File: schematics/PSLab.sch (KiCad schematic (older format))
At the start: 76 parts, among them J1 Programmer, J10 GND, J11 Vbus, J13 D+, J14 D-, J15 External Power, J16 I2C-2, J2 DoublePins, J5 Bluetooth, J6 I2C-1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

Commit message: fix: fiducials for production
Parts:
- TP5, TP6, TP7: footprint Fiducial:Fiducial_0.5mm_Mask1mm -> Fiducial:Fiducial_1mm_Mask2mm
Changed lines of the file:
@@
 F 0 "TP5" V 9731 6083 47  0000 L CNN
 F 1 "Fiducial" V 9818 6083 47  0000 L CNN
-F 2 "Fiducial:Fiducial_0.5mm_Mask1mm" H 9775 6005 60  0001 C CNN
+F 2 "Fiducial:Fiducial_1mm_Mask2mm" H 9775 6005 60  0001 C CNN
 F 3 "" H 9775 6005 60  0001 C CNN
 	1    9775 6005
@@
 F 0 "TP6" V 10176 6083 47  0000 L CNN
 F 1 "Fiducial" V 10263 6083 47  0000 L CNN
-F 2 "Fiducial:Fiducial_0.5mm_Mask1mm" H 10220 6005 60  0001 C CNN
+F 2 "Fiducial:Fiducial_1mm_Mask2mm" H 10220 6005 60  0001 C CNN
 F 3 "" H 10220 6005 60  0001 C CNN
 	1    10220 6005
@@
 F 0 "TP7" V 10626 6083 47  0000 L CNN
 F 1 "Fiducial" V 10713 6083 47  0000 L CNN
-F 2 "Fiducial:Fiducial_0.5mm_Mask1mm" H 10670 6005 60  0001 C CNN
+F 2 "Fiducial:Fiducial_1mm_Mask2mm" H 10670 6005 60  0001 C CNN
 F 3 "" H 10670 6005 60  0001 C CNN
 	1    10670 6005

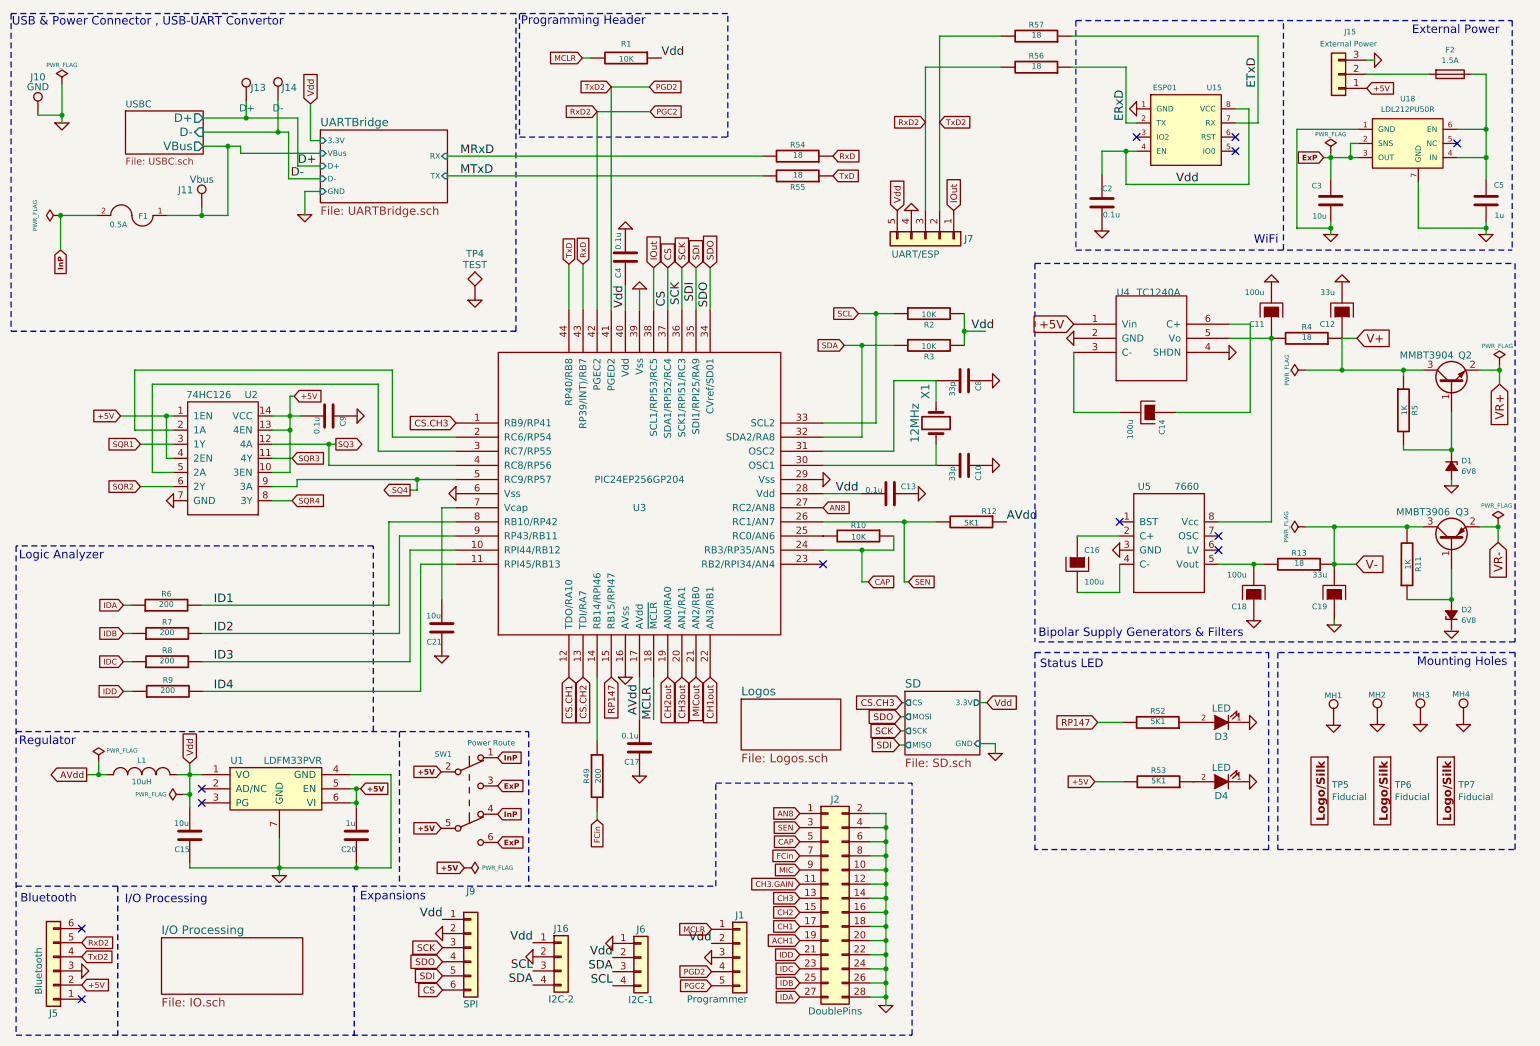
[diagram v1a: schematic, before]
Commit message: fix: line issues in uart ic for external power
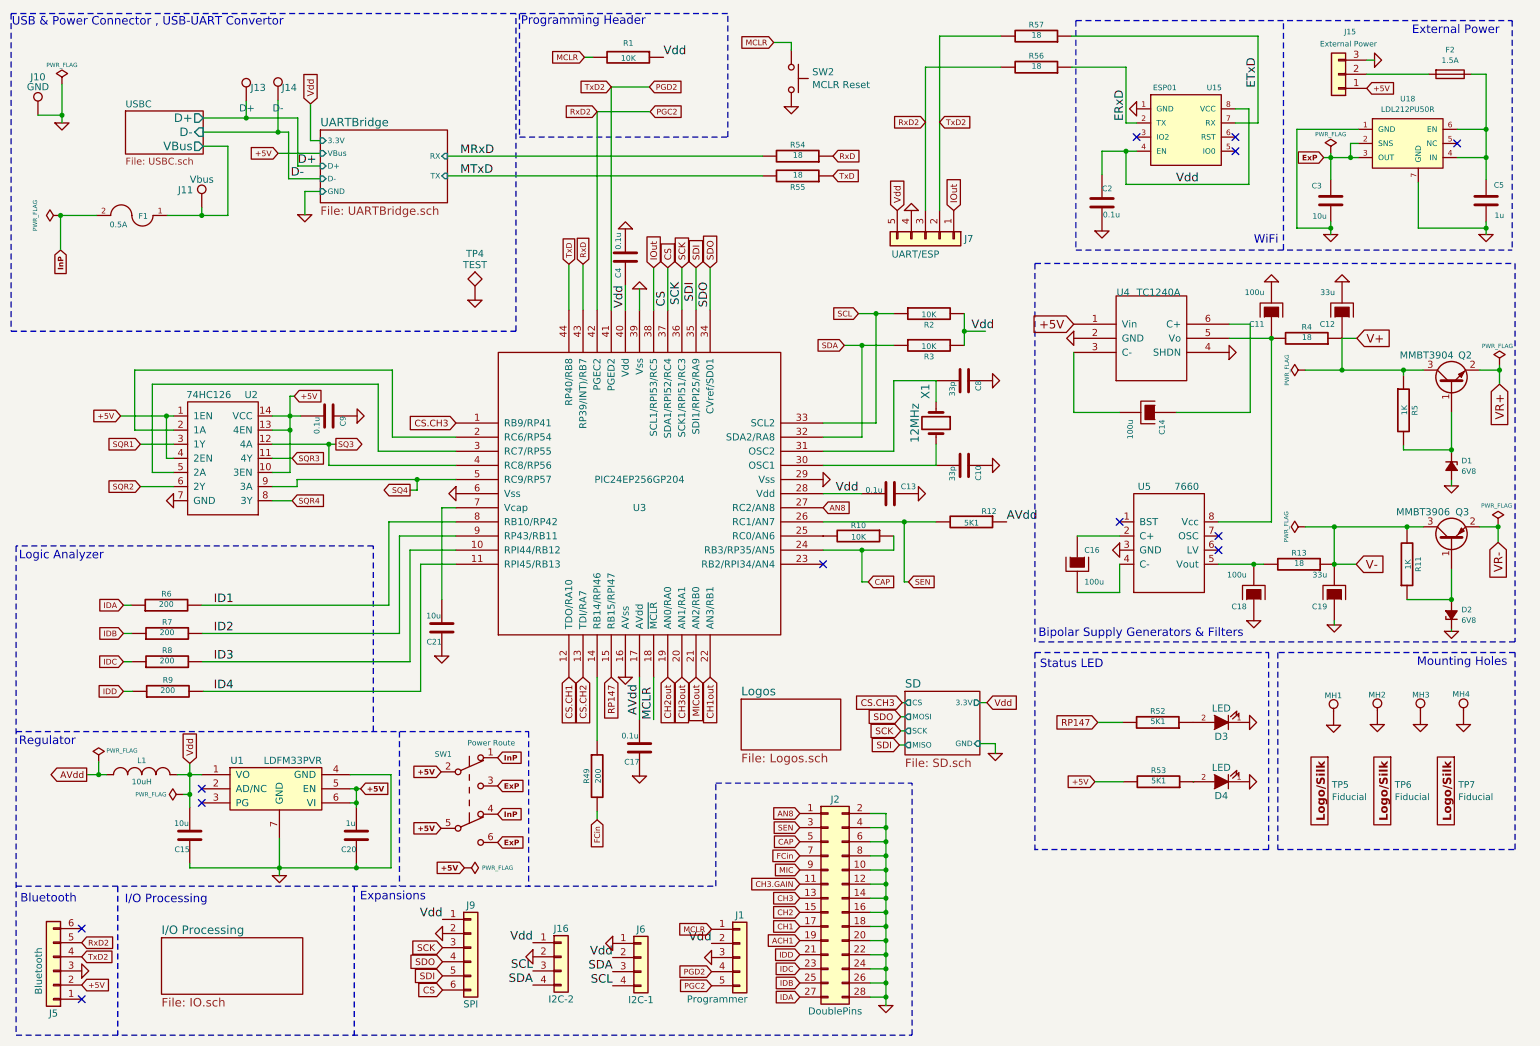
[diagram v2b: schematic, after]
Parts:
- added SW2: MCLR Reset, Button_Switch_SMD:SW_SPST_B3U-1000P, symbol Switch:SW_Push
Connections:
- net GND: now also SW2.2
- net MCLR: now also SW2.1
- net UARTBridge/VBus renamed USBC/VBus
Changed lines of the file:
@@
 L PSLab-rescue:R-RESCUE-proto1 R1
 U 1 1 542164DA
-P 4855 815
-F 0 "R1" V 4755 815 40  0000 C CNN
-F 1 "10K" V 4862 816 40  0000 C CNN
-F 2 "Resistor_SMD:R_0603_1608Metric" V 4785 815 30  0001 C CNN
-F 3 "" H 4855 815 30  0000 C CNN
-	1    4855 815
-	0    1    1    0
-$EndComp
-Text Label 5105 815  0    60   ~ 0
+P 4870 810
+F 0 "R1" V 4770 810 40  0000 C CNN
+F 1 "10K" V 4877 811 40  0000 C CNN
+F 2 "Resistor_SMD:R_0603_1608Metric" V 4800 810 30  0001 C CNN
+F 3 "" H 4870 810 30  0000 C CNN
+	1    4870 810
+	0    1    1    0
+$EndComp
+Text Label 5120 810  0    60   ~ 0
 Vdd
 Text Label 5050 5500 1    60   ~ 0
@@
 Text GLabel 5460 6985 0    40   Input ~ 0
 MCLR
-Text GLabel 4545 815  0    40   Input ~ 0
+Text GLabel 4560 810  0    40   Input ~ 0
 MCLR
 $Comp
@@
 U 1 1 5C4FD974
 P 3755 7115
-F 0 "J9" H 3755 7515 50  0000 C CNN
+F 0 "J9" H 3755 7415 50  0000 C CNN
 F 1 "SPI" H 3755 6715 50  0000 C CNN
 F 2 "Pin_Headers:Pin_Header_Straight_1x06_Pitch2.54mm" H 3755 7115 50  0001 C CNN
@@
 	4650 6150 4650 6210
 Wire Wire Line
-	4605 815  4545 815
+	4620 810  4560 810
 Wire Wire Line
 	7050 3250 7050 3100
@@
 Wire Wire Line
 	2530 1580 2690 1580
-Wire Wire Line
-	2690 1490 2125 1490
-Wire Wire Line
-	2125 1490 2125 1440
-Connection ~ 2035 1440
 Wire Wire Line
 	2390 1115 2390 1340
@@
 	6695 7465 6695 7525
 Wire Wire Line
-	2035 1440 2125 1440
-Wire Wire Line
 	2390 1340 2465 1340
 Wire Wire Line
@@
 	10700 4650 10700 4435
 Connection ~ 10700 4650
+Text GLabel 2390 1490 0    40   Input ~ 0
++5V
+Wire Wire Line
+	2390 1490 2690 1490
+$Comp
+L Switch:SW_Push SW2
+U 1 1 5F5E489E
+P 6025 960
+F 0 "SW2" V 5979 1108 50  0000 L CNN
+F 1 "MCLR Reset" V 6070 1108 50  0000 L CNN
+F 2 "Button_Switch_SMD:SW_SPST_B3U-1000P" H 6025 1160 50  0001 C CNN
+F 3 "~" H 6025 1160 50  0001 C CNN
+	1    6025 960
+	0    1    1    0
+$EndComp
+Text GLabel 5900 705  0    40   Input ~ 0
+MCLR
+Wire Wire Line
+	5900 705  6025 705
+Wire Wire Line
+	6025 705  6025 760
+$Comp
+L PSLab-rescue:GND-RESCUE-proto1 #PWR08
+U 1 1 5F5FC7B8
+P 6025 1160
+F 0 "#PWR08" H 6025 1160 30  0001 C CNN
+F 1 "GND" H 6025 1090 30  0001 C CNN
+F 2 "" H 6025 1160 60  0000 C CNN
+F 3 "" H 6025 1160 60  0000 C CNN
+	1    6025 1160
+	1    0    0    -1
+$EndComp
 $EndSCHEMATC

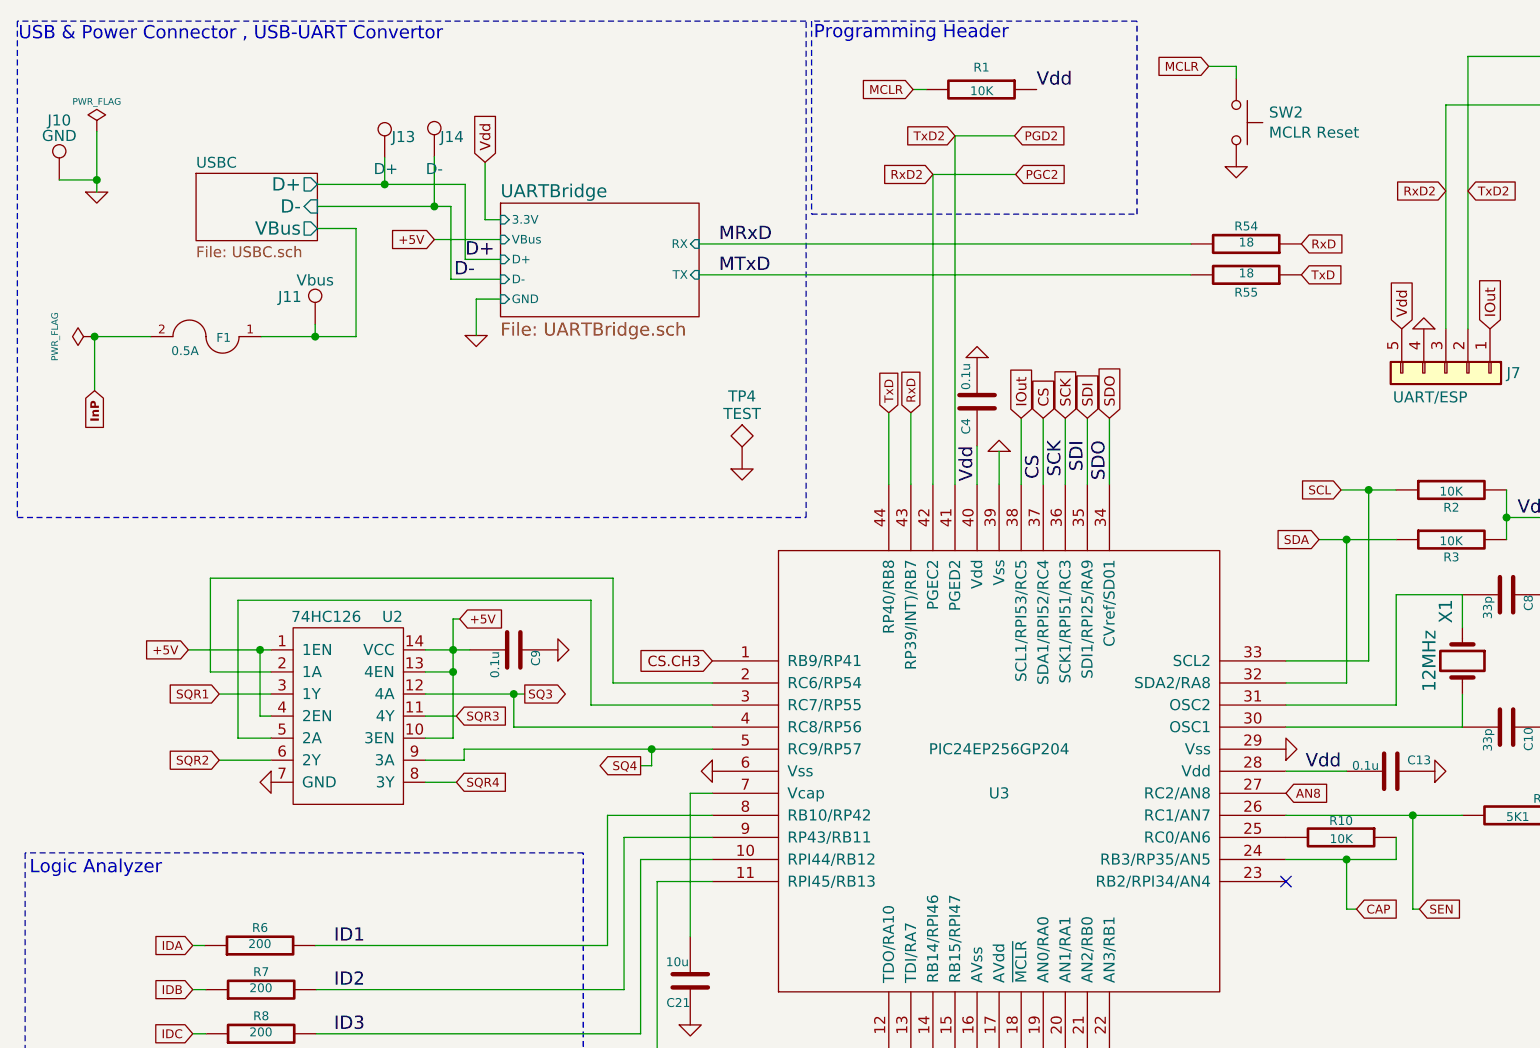
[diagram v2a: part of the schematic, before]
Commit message: feat: added ws2812b led
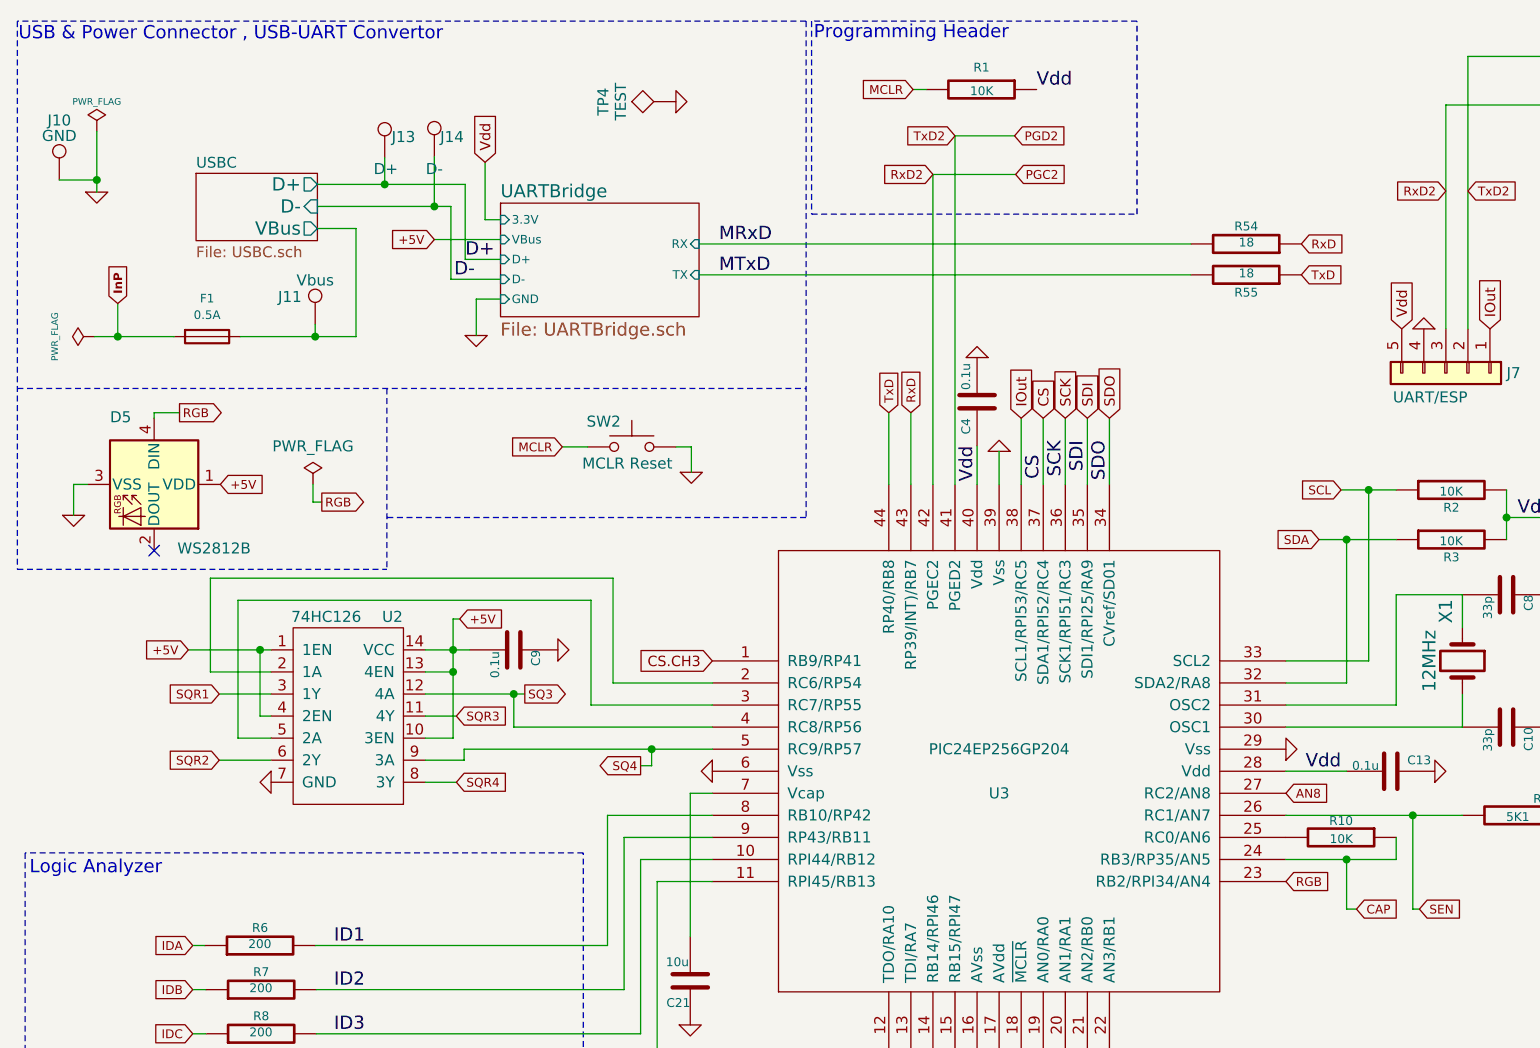
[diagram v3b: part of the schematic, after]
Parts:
- removed F1: 0.5A, Fuse:Fuse_1206_3216Metric, symbol PSLab-rescue:FUSE
- added D5: WS2812B, LED_SMD:LED_WS2812B_PLCC4_5.0x5.0mm_P3.2mm, symbol LED:WS2812B
- added F1: 0.5A, Fuse:Fuse_1206_3216Metric, symbol Device:Fuse
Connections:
- net +5V: now also D5.1 (VDD)
- net GND: now also D5.3 (VSS)
- net InP: now also F1.2
- net USBC/VBus: now also F1.1
- net RGB: now reaches U3.23 (RB2/RPI34/AN4)
- net RGB: now also D5.4 (DIN)
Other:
- moved on the sheet: SW2, TP4
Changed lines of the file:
@@
 Vdd
-$Comp
-L PSLab-rescue:FUSE F1
-U 1 1 54225B8E
-P 1355 1930
-F 0 "F1" H 1275 1935 40  0000 C CNN
-F 1 "0.5A" H 1450 1995 40  0000 C CNN
-F 2 "Fuse:Fuse_1206_3216Metric" H 1355 1930 60  0001 C CNN
-F 3 "" H 1355 1930 60  0000 C CNN
-	1    1355 1930
-	-1   0    0    1
-$EndComp
 $Comp
 L PSLab-rescue:GND-RESCUE-proto1 #PWR01
@@
 L PSLab-rescue:TEST TP4
 U 1 1 5A66B7F8
-P 3785 2530
-F 0 "TP4" H 3785 2830 50  0000 C BNN
-F 1 "TEST" H 3785 2780 50  0000 C CNN
-F 2 "TestPoint:TestPoint_Pad_1.0x1.0mm" H 3785 2530 50  0001 C CNN
-F 3 "" H 3785 2530 50  0001 C CNN
-	1    3785 2530
-	1    0    0    -1
+P 3485 865
+F 0 "TP4" H 3485 1165 50  0000 C BNN
+F 1 "TEST" H 3485 1115 50  0000 C CNN
+F 2 "TestPoint:TestPoint_Pad_1.0x1.0mm" H 3485 865 50  0001 C CNN
+F 3 "" H 3485 865 50  0001 C CNN
+	1    3485 865
+	0    -1   -1   0
 $EndComp
 $Comp
 L PSLab-rescue:GND-RESCUE-proto1 #PWR041
 U 1 1 5A66B8E0
-P 3785 2530
-F 0 "#PWR041" H 3785 2530 30  0001 C CNN
-F 1 "GND" H 3785 2460 30  0001 C CNN
-F 2 "" H 3785 2530 60  0000 C CNN
-F 3 "" H 3785 2530 60  0000 C CNN
-	1    3785 2530
-	1    0    0    -1
+P 3485 865
+F 0 "#PWR041" H 3485 865 30  0001 C CNN
+F 1 "GND" H 3485 795 30  0001 C CNN
+F 2 "" H 3485 865 60  0000 C CNN
+F 3 "" H 3485 865 60  0000 C CNN
+	1    3485 865
+	0    -1   -1   0
 $EndComp
 $Comp
@@
 Text Notes 565  6805 0    60   ~ 0
 Bluetooth
-NoConn ~ 6250 4400
 Text GLabel 2620 1140 1    47   Input ~ 0
 Vdd
@@
 	3175 4100 3650 4100
 Wire Wire Line
-	850  1930 1105 1930
-Connection ~ 850  1930
-Wire Wire Line
-	850  2175 850  1930
+	850  1930 955  1930
 Wire Wire Line
 	5050 5200 5050 5500
@@
 Wire Wire Line
 	8195 5520 8370 5520
-Wire Notes Line
-	500  2750 4075 2750
-Wire Notes Line
-	4075 2750 4075 500
 Wire Notes Line
 	4075 500  500  500
@@
 	1860 1340 2390 1340
 Wire Wire Line
-	1605 1930 1850 1930
-Wire Wire Line
 	2035 1930 2035 1440
 Wire Wire Line
@@
 Wire Wire Line
 	8175 5940 8375 5940
-Wire Notes Line
-	500  500  500  2750
 Wire Wire Line
 	5025 1195 4650 1195
@@
 Wire Wire Line
 	10155 830  10100 830
-Text GLabel 850  2175 3    39   Input ~ 8
+Text GLabel 955  1780 1    39   Input ~ 8
 InP
 Wire Notes Line
@@
 L Switch:SW_Push SW2
 U 1 1 5F5E489E
-P 6025 960
-F 0 "SW2" V 5979 1108 50  0000 L CNN
-F 1 "MCLR Reset" V 6070 1108 50  0000 L CNN
-F 2 "Button_Switch_SMD:SW_SPST_B3U-1000P" H 6025 1160 50  0001 C CNN
-F 3 "~" H 6025 1160 50  0001 C CNN
-	1    6025 960
-	0    1    1    0
-$EndComp
-Text GLabel 5900 705  0    40   Input ~ 0
+P 3285 2430
+F 0 "SW2" H 3080 2545 50  0000 L CNN
+F 1 "MCLR Reset" H 3060 2355 50  0000 L CNN
+F 2 "Button_Switch_SMD:SW_SPST_B3U-1000P" H 3285 2630 50  0001 C CNN
+F 3 "~" H 3285 2630 50  0001 C CNN
+	1    3285 2430
+	1    0    0    -1
+$EndComp
+Text GLabel 2970 2430 0    40   Input ~ 0
 MCLR
-Wire Wire Line
-	5900 705  6025 705
-Wire Wire Line
-	6025 705  6025 760
 $Comp
 L PSLab-rescue:GND-RESCUE-proto1 #PWR08
 U 1 1 5F5FC7B8
-P 6025 1160
-F 0 "#PWR08" H 6025 1160 30  0001 C CNN
-F 1 "GND" H 6025 1090 30  0001 C CNN
-F 2 "" H 6025 1160 60  0000 C CNN
-F 3 "" H 6025 1160 60  0000 C CNN
-	1    6025 1160
-	1    0    0    -1
-$EndComp
+P 3555 2545
+F 0 "#PWR08" H 3555 2545 30  0001 C CNN
+F 1 "GND" H 3555 2475 30  0001 C CNN
+F 2 "" H 3555 2545 60  0000 C CNN
+F 3 "" H 3555 2545 60  0000 C CNN
+	1    3555 2545
+	1    0    0    -1
+$EndComp
+Wire Wire Line
+	955  1780 955  1930
+Connection ~ 955  1930
+$Comp
+L Device:Fuse F1
+U 1 1 5F5AC6B6
+P 1360 1930
+F 0 "F1" V 1187 1930 39  0000 C CNN
+F 1 "0.5A" V 1262 1930 39  0000 C CNN
+F 2 "Fuse:Fuse_1206_3216Metric" V 1290 1930 50  0001 C CNN
+F 3 "https://www.mouser.fi/datasheet/2/240/Littelfuse_PTC_1812L_Datasheet.pdf-693388.pdf" H 1360 1930 50  0001 C CNN
+	1    1360 1930
+	0    1    1    0
+$EndComp
+Wire Wire Line
+	955  1930 1210 1930
+Wire Wire Line
+	1510 1930 1850 1930
+Wire Notes Line
+	500  2165 4075 2165
+Wire Notes Line
+	4075 500  4075 2750
+Wire Wire Line
+	2970 2430 3085 2430
+Wire Wire Line
+	3485 2430 3555 2430
+Wire Wire Line
+	3555 2430 3555 2545
+$Comp
+L LED:WS2812B D5
+U 1 1 5F65D829
+P 1120 2600
+F 0 "D5" V 815 2400 50  0000 L CNN
+F 1 "WS2812B" V 1410 2705 50  0000 L CNN
+F 2 "LED_SMD:LED_WS2812B_PLCC4_5.0x5.0mm_P3.2mm" H 1170 2300 50  0001 L TNN
+F 3 "https://cdn-shop.adafruit.com/datasheets/WS2812B.pdf" H 1220 2225 50  0001 L TNN
+	1    1120 2600
+	0    1    1    0
+$EndComp
+Wire Notes Line
+	500  2985 2175 2985
+Wire Notes Line
+	500  500  500  2985
+Wire Notes Line
+	4075 2750 2175 2750
+Wire Notes Line
+	2175 2165 2175 2985
+$Comp
+L PSLab-rescue:GND-RESCUE-proto1 #PWR033
+U 1 1 5F6AB933
+P 755 2740
+F 0 "#PWR033" H 755 2740 30  0001 C CNN
+F 1 "GND" H 755 2670 30  0001 C CNN
+F 2 "" H 755 2740 60  0000 C CNN
+F 3 "" H 755 2740 60  0000 C CNN
+	1    755  2740
+	1    0    0    -1
+$EndComp
+Wire Wire Line
+	755  2740 755  2600
+Wire Wire Line
+	755  2600 820  2600
+NoConn ~ 1120 2900
+Text GLabel 1420 2600 2    40   Input ~ 0
++5V
+Wire Wire Line
+	1120 2275 1120 2300
+Wire Wire Line
+	1235 2275 1120 2275
+Text GLabel 6250 4400 2    40   Input ~ 0
+RGB
+Text GLabel 1235 2275 2    40   Output ~ 0
+RGB
+$Comp
+L power:PWR_FLAG #FLG0105
+U 1 1 5F75FF82
+P 1840 2600
+F 0 "#FLG0105" H 1840 2675 50  0001 C CNN
+F 1 "PWR_FLAG" H 1840 2773 50  0000 C CNN
+F 2 "" H 1840 2600 50  0001 C CNN
+F 3 "~" H 1840 2600 50  0001 C CNN
+	1    1840 2600
+	1    0    0    -1
+$EndComp
+Text GLabel 1880 2680 2    40   Output ~ 0
+RGB
+Wire Wire Line
+	1840 2600 1840 2680
+Wire Wire Line
+	1840 2680 1880 2680
 $EndSCHEMATC
